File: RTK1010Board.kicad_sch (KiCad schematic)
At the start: 53 parts, among them J1 SMA, J2 IPEX, J3 USB_OTG, U1 RTK-1010, U2 MCP1700-3002E_SOT23, U3 MCP1700-3002E_SOT23, U4 ESP32-S2-MINI-1

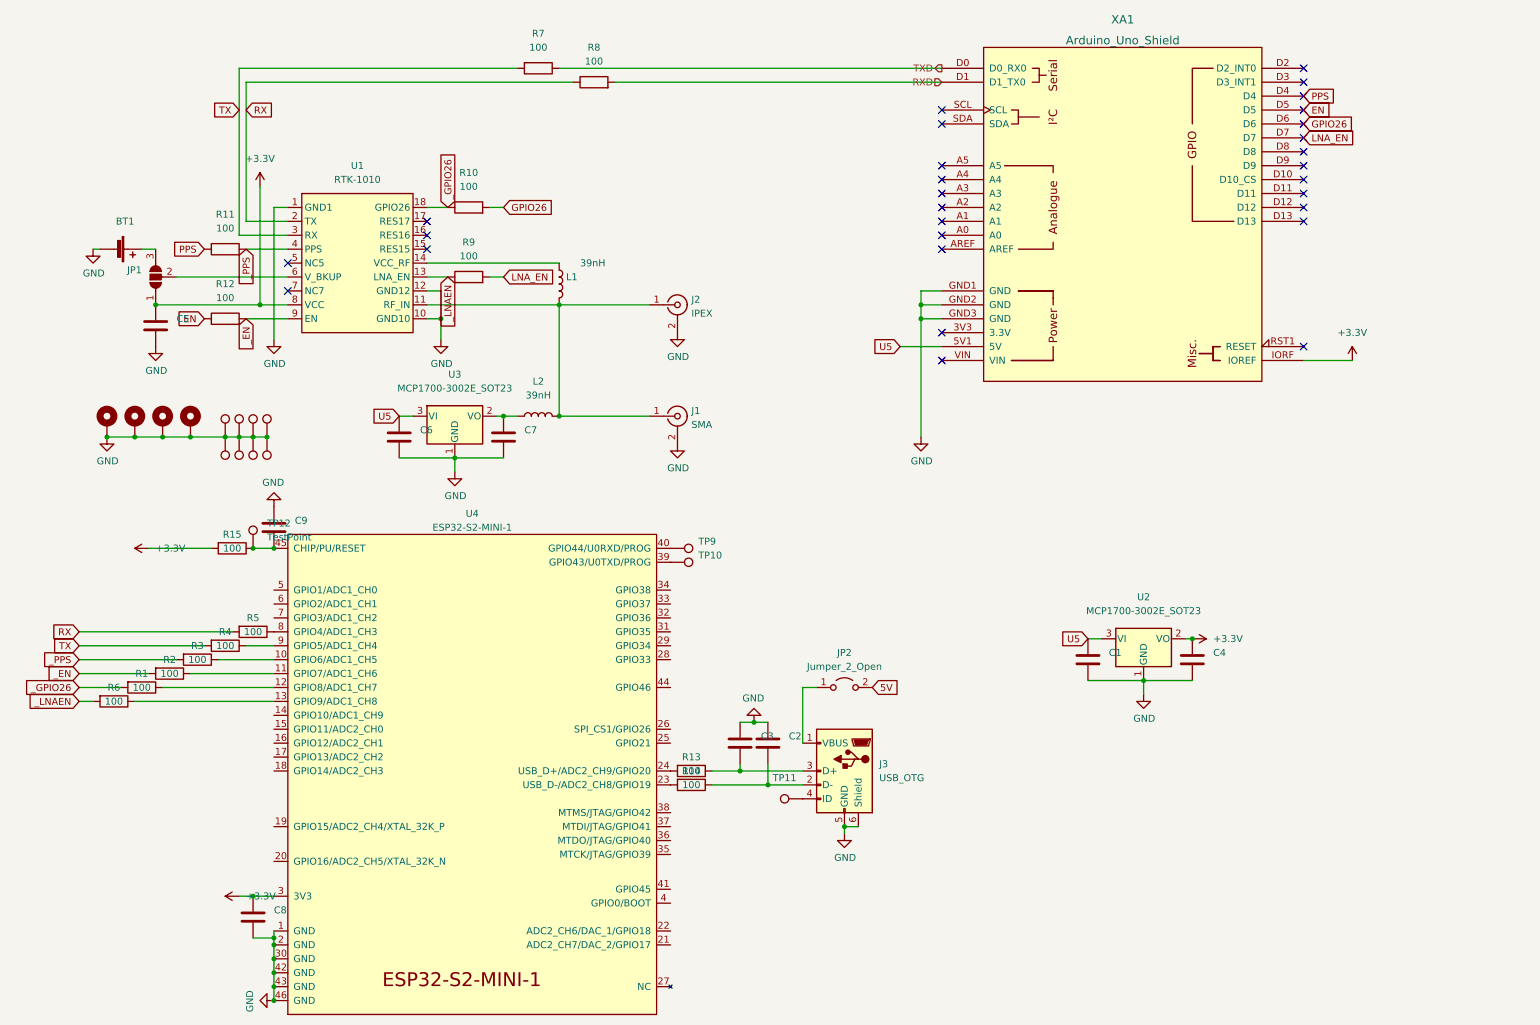
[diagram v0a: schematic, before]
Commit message: ESP32-S2 mini replaced by WROVER module
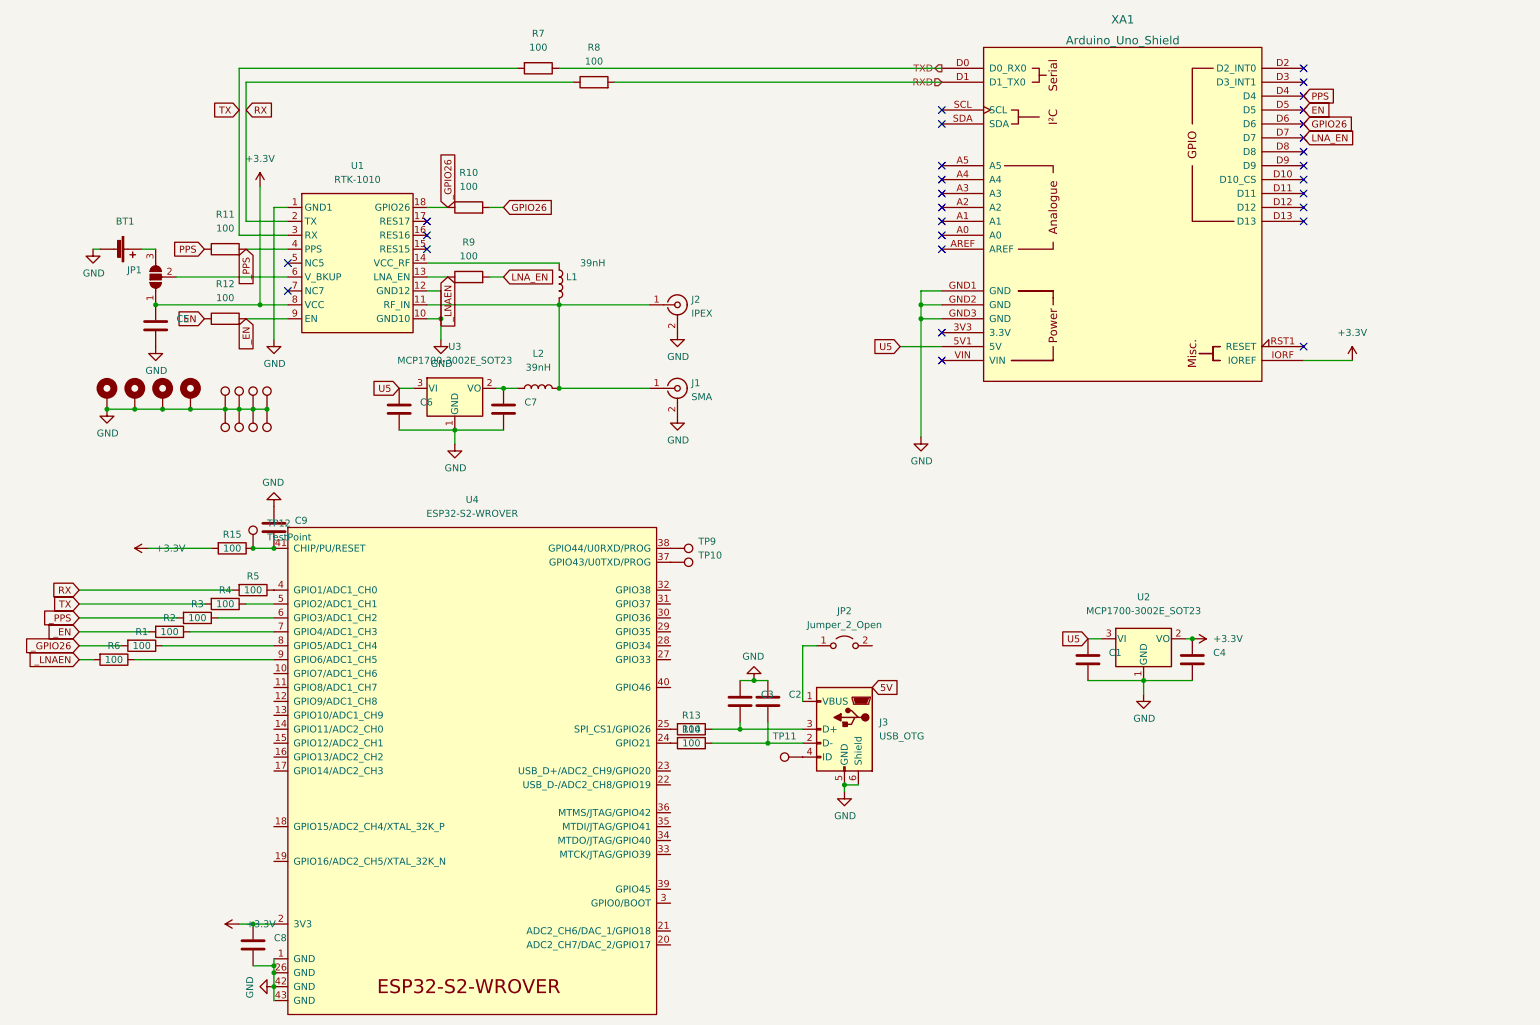
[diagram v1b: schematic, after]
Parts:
- removed U4: ESP32-S2-MINI-1, Espressif:ESP32-S2-MINI-1, symbol Espressif:ESP32-S2-MINI-1
- added U4: ESP32-S2-WROVER, Espressif:ESP32-S2-WROVER, symbol Espressif:ESP32-S2-WROVER
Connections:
- net +3V3: now also U4.2 (3V3)
- net 5V: no longer JP2.2 (B)
- net GND: now also U4.1 (GND), U4.26 (GND), U4.42 (GND), U4.43 (GND)
- net at R2.1: now also U4.7 (GPIO4/ADC1_CH3)
- net at TP10.1: now also U4.37 (GPIO43/U0TXD/PROG)
- net at C9.2, R15.1, TP12.1: now also U4.41 (CHIP/PU/RESET)
- net at TP9.1: now also U4.38 (GPIO44/U0RXD/PROG)
- net at R5.1: now also U4.4 (GPIO1/ADC1_CH0)
- net at R1.1: now also U4.8 (GPIO5/ADC1_CH4)
- net at R3.1: now also U4.6 (GPIO3/ADC1_CH2)
- net at R13.2: now also U4.25 (SPI_CS1/GPIO26)
- net at R14.2: now also U4.24 (GPIO21)
- net at R6.1: now also U4.9 (GPIO6/ADC1_CH5)
- net at R4.1: now also U4.5 (GPIO2/ADC1_CH1)
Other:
- moved on the sheet: C2, C3, C6, C7, C8, J1, J3, JP2, L2, R1, R13, R14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

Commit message: some more small changes
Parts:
- added C10, C11: 10uF, Capacitor_Tantalum_SMD:CP_EIA-7132-20_AVX-U_Pad2.72x3.50mm_HandSolder, symbol Device:C_Polarized_Small
- BT1: value Battery_Cell -> 3.3V
- JP2: value Jumper_2_Open -> USB power
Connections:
- net +3V3: now also C11.1
- net 5V: now also JP2.2 (B)
- net GND: now also C10.2, C11.2
- net _PPS: no longer R11.2, U1.4 (PPS)
- net ULAN: now reaches C7.1, L2.1, U3.2 (VO)
- net ULAN: now also C10.1
- new net: R11.2, U1.4 (PPS)
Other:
- note added: "3.3V Power Supply (Optional)"
- note added: "Backup Batterie (Optional)"
- note added: "ESP32 WRover (Optional)"
- note added: "LNA Power Supply (Optional)"
- moved on the sheet: BT1, C1, C2, C3, C4, C5, C6, C7, C8, C9, J1, J2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

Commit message: -
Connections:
- net _PPS: now also R11.2, U1.4 (PPS)
- net EN: no longer names the net of R12.1, XA1.D5
- net GPIO26: no longer names the net of R10.2, XA1.D6
- net LNA_EN: no longer names the net of R9.2, XA1.D7
- net PPS: no longer names the net of R11.1, XA1.D4
- net ULAN renamed ULNA
- no-connect marks 29 -> 25
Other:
- note added: "Arduino Connector (Optional)"
- moved on the sheet: R10, R11, R12, R7, R8, R9

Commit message: -
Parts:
- added TP_GND1: TestPoint, TestPoint:TestPoint_Pad_D2.0mm, symbol Connector:TestPoint
- renumbered TP12 to TP_EN1, TP11 to TP_OTG1, TP9 to TP_U0RXD1, TP10 to TP_U0TXD1
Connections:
- net GND: now also TP_GND1.1
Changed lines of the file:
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@@
+    (stroke (width 0) (type default) (color 0 0 0 0))
+  )
+  (wire (pts (xy 132.08 102.87) (xy 133.35 102.87))
     (stroke (width 0) (type default) (color 0 0 0 0))
   )
@@
   (symbol (lib_id "Connector:TestPoint") (at 133.35 111.76 270) (unit 1)
     (in_bom yes) (on_board yes) (fields_autoplaced)
-    (property "Reference" "TP10" (id 0) (at 138.43 110.4899 90)
+    (property "Reference" "TP_U0TXD1" (id 0) (at 138.43 111.7599 90)
       (effects (font (size 1.27 1.27)) (justify left))
     )
@@
     (pin "2")
   )
+  (symbol (lib_id "Connector:TestPoint") (at 133.35 102.87 270) (unit 1)
+    (in_bom yes) (on_board yes) (fields_autoplaced)
+    (property "Reference" "TP_GND1" (id 0) (at 138.43 102.8699 90)
+      (effects (font (size 1.27 1.27)) (justify left))
+    )
+    (property "Value" "TestPoint" (id 1) (at 138.43 104.1399 90)
+      (effects (font (size 1.27 1.27)) (justify left) hide)
+    )
+    (property "Footprint" "TestPoint:TestPoint_Pad_D2.0mm" (id 2) (at 133.35 107.95 0)
+      (effects (font (size 1.27 1.27)) hide)
+    )
+    (property "Datasheet" "~" (id 3) (at 133.35 107.95 0)
+      (effects (font (size 1.27 1.27)) hide)
+    )
+    (pin "1")
+  )
   (symbol (lib_id "Device:R") (at 257.81 33.02 270) (unit 1)
     (in_bom yes) (on_board yes)
@@
     (pin "1")
     (pin "2")
+  )
+  (symbol (lib_id "power:GND") (at 132.08 102.87 270) (unit 1)
+    (in_bom yes) (on_board yes)
+    (property "Reference" "#PWR0120" (id 0) (at 125.73 102.87 0)
+      (effects (font (size 1.27 1.27)) hide)
+    )
+    (property "Value" "GND" (id 1) (at 130.81 107.95 0))
+    (property "Footprint" "" (id 2) (at 132.08 102.87 0)
+      (effects (font (size 1.27 1.27)) hide)
+    )
+    (property "Datasheet" "" (id 3) (at 132.08 102.87 0)
+      (effects (font (size 1.27 1.27)) hide)
+    )
+    (pin "1")
   )
   (symbol (lib_id "Regulator_Linear:MCP1700-3002E_SOT23") (at 196.85 147.32 0) (unit 1)
@@
   (symbol (lib_id "Connector:TestPoint") (at 133.35 109.22 270) (unit 1)
     (in_bom yes) (on_board yes) (fields_autoplaced)
-    (property "Reference" "TP9" (id 0) (at 138.43 107.9499 90)
+    (property "Reference" "TP_U0RXD1" (id 0) (at 138.43 109.2199 90)
       (effects (font (size 1.27 1.27)) (justify left))
     )
@@
   )
   (symbol (lib_id "Connector:TestPoint") (at 57.15 109.22 0) (unit 1)
-    (in_bom yes) (on_board yes) (fields_autoplaced)
-    (property "Reference" "TP12" (id 0) (at 59.69 104.6479 0)
+    (in_bom yes) (on_board yes)
+    (property "Reference" "TP_EN1" (id 0) (at 52.07 104.14 0)
       (effects (font (size 1.27 1.27)) (justify left))
     )
     (property "Value" "TestPoint" (id 1) (at 59.69 107.1879 0)
-      (effects (font (size 1.27 1.27)) (justify left))
+      (effects (font (size 1.27 1.27)) (justify left) hide)
     )
     (property "Footprint" "TestPoint:TestPoint_Pad_D2.0mm" (id 2) (at 62.23 109.22 0)
@@
     )
     (property "Value" "USB_OTG" (id 1) (at 152.4 152.4 0)
-      (effects (font (size 1.27 1.27)) (justify right))
+      (effects (font (size 1.27 1.27)) (justify right) hide)
     )
     (property "Footprint" "Connector_USB:USB_Micro-B_Amphenol_10118194_Horizontal" (id 2) (at 161.29 143.51 0)
@@
   )
   (symbol (lib_id "Connector:TestPoint") (at 157.48 147.32 90) (unit 1)
-    (in_bom yes) (on_board yes) (fields_autoplaced)
-    (property "Reference" "TP11" (id 0) (at 154.178 143.51 90))
+    (in_bom yes) (on_board yes)
+    (property "Reference" "TP_OTG1" (id 0) (at 152.4 149.86 90))
     (property "Value" "TestPoint" (id 1) (at 152.4 146.0501 90)
       (effects (font (size 1.27 1.27)) (justify left) hide)
@@
       (reference "#PWR0119") (unit 1) (value "+3.3V") (footprint "")
     )
+    (path "/33704ed7-dfff-4148-a0b5-dd66191d0243"
+      (reference "#PWR0120") (unit 1) (value "GND") (footprint "")
+    )
     (path "/7deb6910-d13f-42dd-ab27-34cfe2ced14d"
       (reference "BT1") (unit 1) (value "3.3V") (footprint "Battery:BatteryHolder_Keystone_1058_1x2032")
@@
       (reference "TP8") (unit 1) (value "TestPoint") (footprint "TestPoint:TestPoint_Loop_D2.50mm_Drill1.0mm")
     )
+    (path "/6da78148-93e7-42d5-99a0-aa7c10250ff5"
+      (reference "TP_EN1") (unit 1) (value "TestPoint") (footprint "TestPoint:TestPoint_Pad_D2.0mm")
+    )
+    (path "/225f933d-0727-401c-981a-5fd8cac707fb"
+      (reference "TP_GND1") (unit 1) (value "TestPoint") (footprint "TestPoint:TestPoint_Pad_D2.0mm")
+    )
+    (path "/c6f18060-b6f8-4633-ae2f-7095d4ae93f2"
+      (reference "TP_OTG1") (unit 1) (value "TestPoint") (footprint "TestPoint:TestPoint_Pad_D2.0mm")
+    )
     (path "/38ba78ff-d75d-44cf-a39f-5a065ded5c39"
-      (reference "TP9") (unit 1) (value "TestPoint") (footprint "TestPoint:TestPoint_Pad_D2.0mm")
+      (reference "TP_U0RXD1") (unit 1) (value "TestPoint") (footprint "TestPoint:TestPoint_Pad_D2.0mm")
     )
     (path "/1722a3d5-4a55-4f40-9de5-ed05b8a82c22"
-      (reference "TP10") (unit 1) (value "TestPoint") (footprint "TestPoint:TestPoint_Pad_D2.0mm")
-    )
-    (path "/c6f18060-b6f8-4633-ae2f-7095d4ae93f2"
-      (reference "TP11") (unit 1) (value "TestPoint") (footprint "TestPoint:TestPoint_Pad_D2.0mm")
-    )
-    (path "/6da78148-93e7-42d5-99a0-aa7c10250ff5"
-      (reference "TP12") (unit 1) (value "TestPoint") (footprint "TestPoint:TestPoint_Pad_D2.0mm")
+      (reference "TP_U0TXD1") (unit 1) (value "TestPoint") (footprint "TestPoint:TestPoint_Pad_D2.0mm")
     )
     (path "/3589c26d-9a04-4339-94e9-ce4b2221d6be"

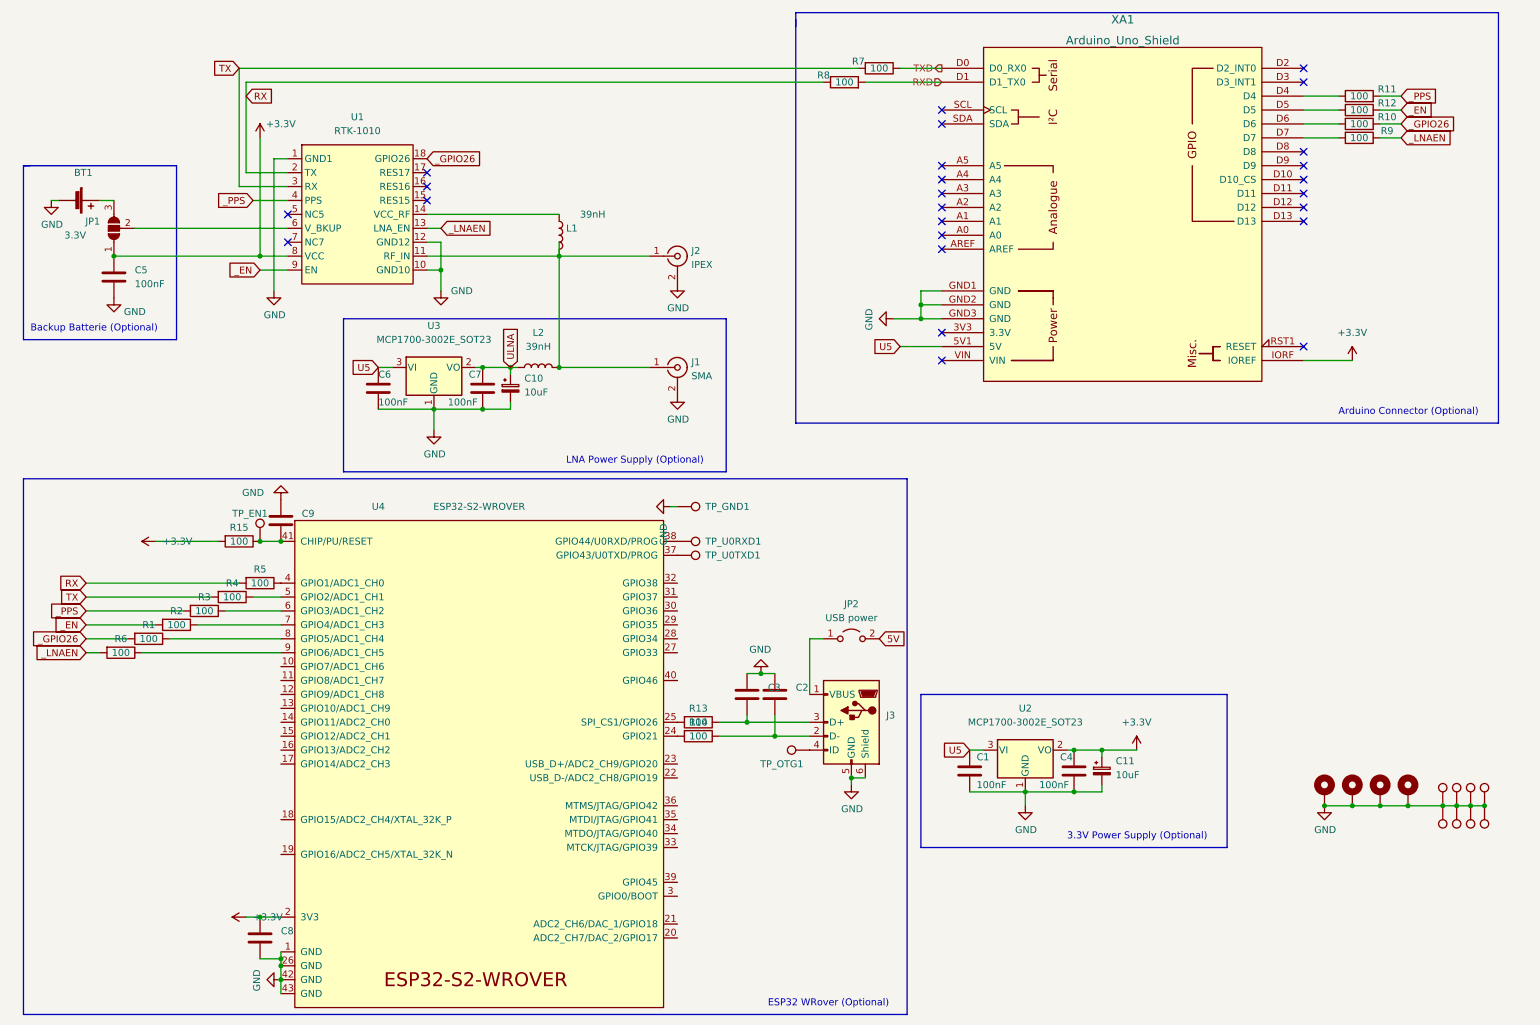
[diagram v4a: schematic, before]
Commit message: bno055 added
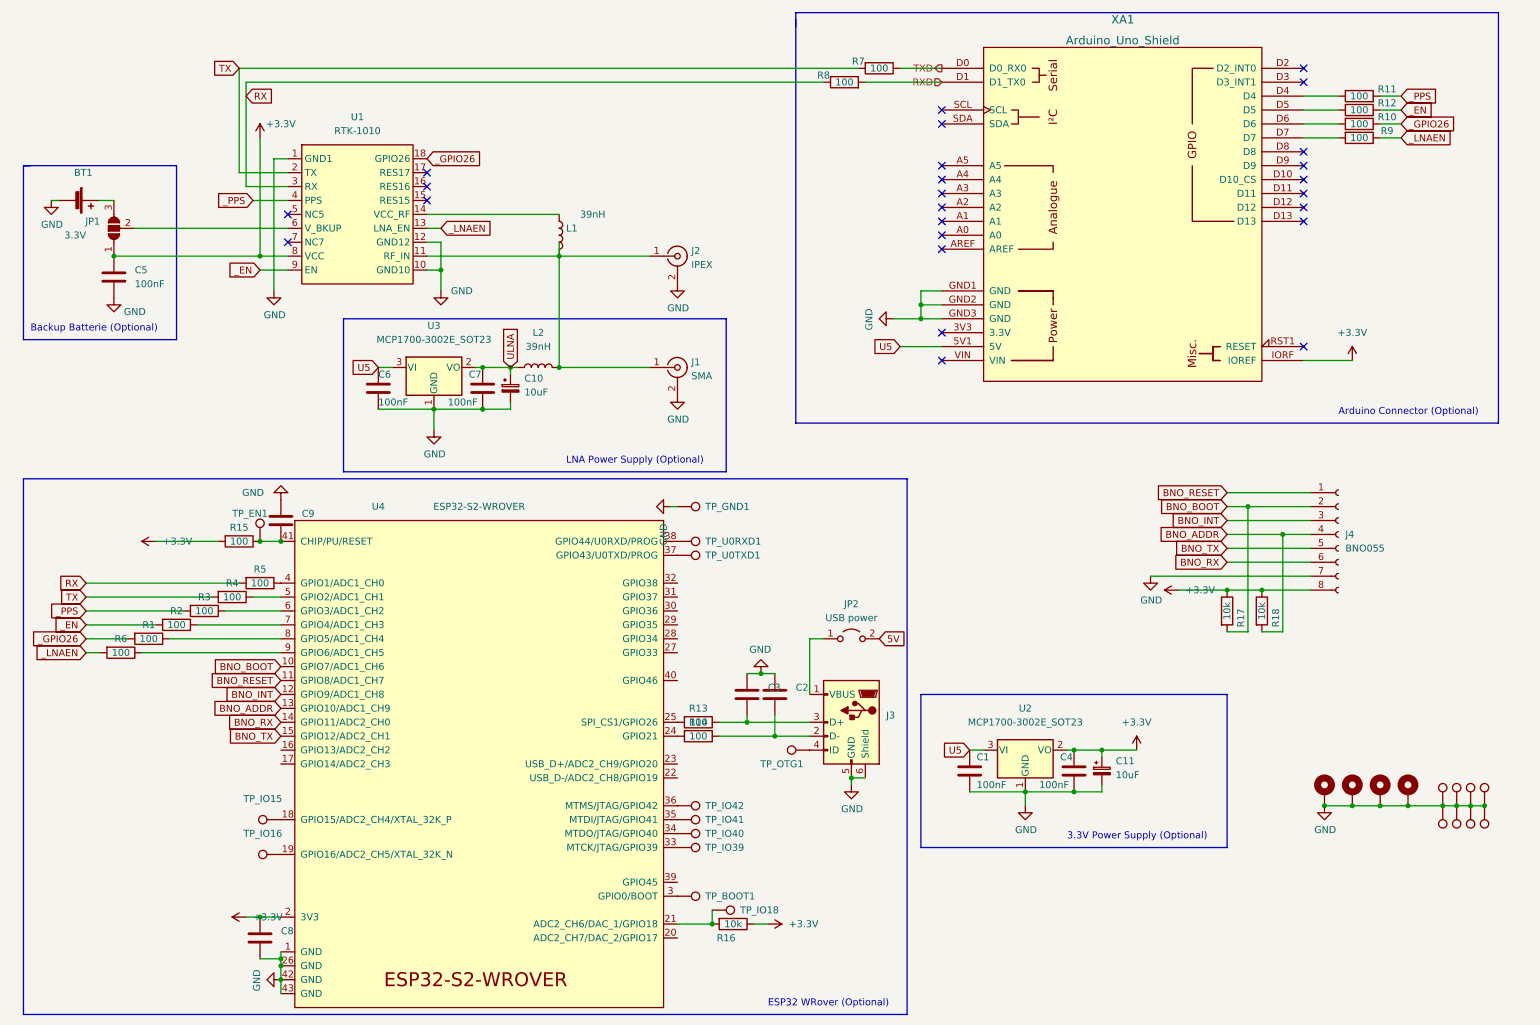
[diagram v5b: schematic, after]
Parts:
- added J4: BNO055, Connector_PinSocket_2.54mm:PinSocket_1x08_P2.54mm_Vertical_SMD_Pin1Right, symbol Connector:Conn_01x08_Female
- added R16, R17, R18: 10k, Resistor_SMD:R_0805_2012Metric_Pad1.20x1.40mm_HandSolder, symbol Device:R
- added TP_BOOT1, TP_IO15, TP_IO16, TP_IO18, TP_IO39, TP_IO40, TP_IO41, TP_IO42: TestPoint, TestPoint:TestPoint_Pad_D2.0mm, symbol Connector:TestPoint
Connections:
- net +3V3: now also J4.8 (Pin_8), R16.1, R17.1, R18.1
- net GND: now also J4.7 (Pin_7)
- net RX: now also U1.3 (RX); no longer U1.2 (TX)
- net TX: now also U1.2 (TX); no longer U1.3 (RX)
- net BNO_BOOT: now reaches U4.10 (GPIO7/ADC1_CH6)
- net BNO_BOOT: now also J4.2 (Pin_2), R17.2
- net BNO_RESET: now reaches U4.11 (GPIO8/ADC1_CH7)
- net BNO_RESET: now also J4.1 (Pin_1)
- net BNO_INT: now reaches U4.12 (GPIO9/ADC1_CH8)
- net BNO_INT: now also J4.3 (Pin_3)
- net BNO_ADDR: now reaches U4.13 (GPIO10/ADC1_CH9)
- net BNO_ADDR: now also J4.4 (Pin_4), R18.2
- net BNO_RX: now reaches U4.14 (GPIO11/ADC2_CH0)
- net BNO_RX: now also J4.6 (Pin_6)
- net BNO_TX: now reaches U4.15 (GPIO12/ADC2_CH1)
- net BNO_TX: now also J4.5 (Pin_5)
- net at U4.18 (GPIO15/ADC2_CH4/XTAL_32K_P): now also TP_IO15.1
- net at U4.19 (GPIO16/ADC2_CH5/XTAL_32K_N): now also TP_IO16.1
- net at U4.21 (ADC2_CH6/DAC_1/GPIO18): now also R16.2, TP_IO18.1
- net at U4.3 (GPIO0/BOOT): now also TP_BOOT1.1
- net at U4.33 (MTCK/JTAG/GPIO39): now also TP_IO39.1
- net at U4.34 (MTDO/JTAG/GPIO40): now also TP_IO40.1
- net at U4.35 (MTDI/JTAG/GPIO41): now also TP_IO41.1
- net at U4.36 (MTMS/JTAG/GPIO42): now also TP_IO42.1
